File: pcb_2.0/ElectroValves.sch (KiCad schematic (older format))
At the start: 53 parts, among them P2 Conn_01x04_Female, Q1 PN2222, Q2 PN2222, Q6 PN2222, Q7 PN2222, U11 AQH3223AX, U12 AQH3223AX, U19 AQH3223AX, U20 AQH3223AX, U3 TLP240D, U4 TLP240D, U5 TLP240D, U6 TLP240D, U7 TLP240D, U8 TLP240D

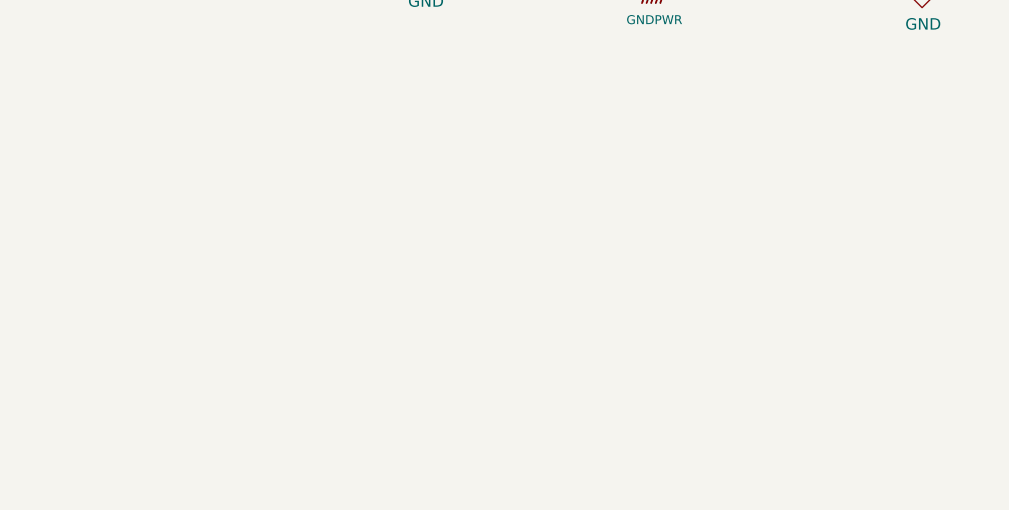
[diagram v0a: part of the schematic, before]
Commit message: driver for motor eliminated
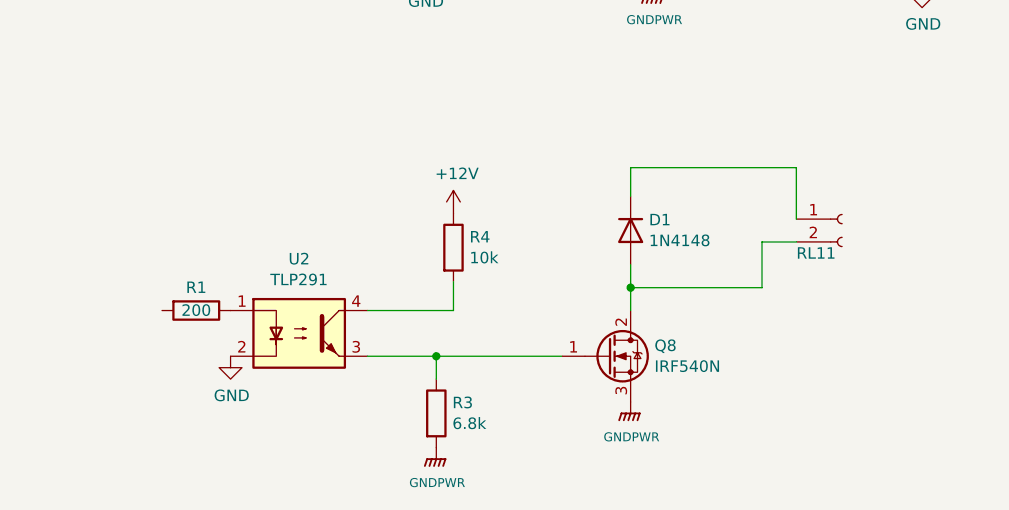
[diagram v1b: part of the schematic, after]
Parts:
- added D1: 1N4148, Diode_THT:D_DO-35_SOD27_P7.62mm_Horizontal, symbol Diode:1N4148
- added Q8: IRF540N, Package_TO_SOT_THT:TO-220-3_Vertical, symbol Transistor_FET:IRF540N
- added R1: 200, symbol Device:R
- added R3: 6.8k, symbol Device:R
- added R4: 10k, symbol Device:R
- added RL11: Conn_01x04_Female, Connector_Phoenix_MC:PhoenixContact_MC_1,5_2-G-3.81_1x02_P3.81mm_Horizontal, symbol BarrelConnector:Conn_01x02_Female
- added U2: TLP291, Package_SO:SOIC-4_4.55x2.6mm_P1.27mm, symbol Isolator:TLP291
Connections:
- net GND: now also U2.2
- net GNDPWR: now also Q8.3 (S), R3.2
- new net: R1.1, U2.1
- new net: Q8.1 (G), R3.1, U2.3
- new net: R4.2, U2.4
- new net: D1.2 (A), Q8.2 (D), RL11.2 (Pin_2)
- new net: D1.1 (K), RL11.1 (Pin_1)
- new net +12V: R4.1
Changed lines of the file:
@@
 $EndDescr
-$Comp
-L SolidStateRelay:TLP240D U3
-U 1 1 5E992915
-P 2850 1700
-F 0 "U3" H 2850 2025 50  0000 C CNN
-F 1 "TLP240D" H 2850 1934 50  0000 C CNN
-F 2 "SMD:TLP240D_TP1" H 2650 1500 50  0001 L CIN
-F 3 "https://toshiba.semicon-storage.com/info/docget.jsp?did=13993&prodName=TLP240D" H 2800 1700 50  0001 L CNN
-F 4 "TLP240D(TP1FCT-ND" H 2850 1700 50  0001 C CNN "DigiKey"
-	1    2850 1700
-	1    0    0    -1
-$EndComp
-$Comp
-L SolidStateRelay:TLP240D U4
-U 1 1 5E996503
-P 5025 1700
-F 0 "U4" H 5025 2025 50  0000 C CNN
-F 1 "TLP240D" H 5025 1934 50  0000 C CNN
-F 2 "SMD:TLP240D_TP1" H 4825 1500 50  0001 L CIN
-F 3 "" H 4975 1700 50  0001 L CNN
-F 4 "TLP240D(TP1FCT-ND" H 5025 1700 50  0001 C CNN "DigiKey"
-	1    5025 1700
-	1    0    0    -1
-$EndComp
-$Comp
-L SolidStateRelay:TLP240D U5
-U 1 1 5E9983C1
-P 2850 3475
-F 0 "U5" H 2850 3800 50  0000 C CNN
-F 1 "TLP240D" H 2850 3709 50  0000 C CNN
-F 2 "SMD:TLP240D_TP1" H 2650 3275 50  0001 L CIN
-F 3 "" H 2800 3475 50  0001 L CNN
-F 4 "TLP240D(TP1FCT-ND" H 2850 3475 50  0001 C CNN "DigiKey"
-	1    2850 3475
-	1    0    0    -1
-$EndComp
-$Comp
-L SolidStateRelay:TLP240D U6
-U 1 1 5E9983C7
-P 5025 3525
-F 0 "U6" H 5025 3850 50  0000 C CNN
-F 1 "TLP240D" H 5025 3759 50  0000 C CNN
-F 2 "SMD:TLP240D_TP1" H 4825 3325 50  0001 L CIN
-F 3 "" H 4975 3525 50  0001 L CNN
-F 4 "TLP240D(TP1FCT-ND" H 5025 3525 50  0001 C CNN "DigiKey"
-	1    5025 3525
-	1    0    0    -1
-$EndComp
 $Comp
 L SolidStateRelay:TLP240D U7
@@
 F 4 "TLP240D(TP1FCT-ND" H 2850 5200 50  0001 C CNN "DigiKey"
 	1    2850 5200
-	1    0    0    -1
-$EndComp
-$Comp
-L SolidStateRelay:TLP240D U8
-U 1 1 5E99CC75
-P 5025 5300
-F 0 "U8" H 5025 5625 50  0000 C CNN
-F 1 "TLP240D" H 5025 5534 50  0000 C CNN
-F 2 "SMD:TLP240D_TP1" H 4825 5100 50  0001 L CIN
-F 3 "" H 4975 5300 50  0001 L CNN
-F 4 "TLP240D(TP1FCT-ND" H 5025 5300 50  0001 C CNN "DigiKey"
-	1    5025 5300
 	1    0    0    -1
 $EndComp
@@
 Text Label 6925 5650 0    50   ~ 0
 R16
+$Comp
+L SolidStateRelay:TLP240D U8
+U 1 1 5E99CC75
+P 5025 5300
+F 0 "U8" H 5025 5625 50  0000 C CNN
+F 1 "TLP240D" H 5025 5534 50  0000 C CNN
+F 2 "SMD:TLP240D_TP1" H 4825 5100 50  0001 L CIN
+F 3 "" H 4975 5300 50  0001 L CNN
+F 4 "TLP240D(TP1FCT-ND" H 5025 5300 50  0001 C CNN "DigiKey"
+	1    5025 5300
+	1    0    0    -1
+$EndComp
+$Comp
+L SolidStateRelay:TLP240D U6
+U 1 1 5E9983C7
+P 5025 3525
+F 0 "U6" H 5025 3850 50  0000 C CNN
+F 1 "TLP240D" H 5025 3759 50  0000 C CNN
+F 2 "SMD:TLP240D_TP1" H 4825 3325 50  0001 L CIN
+F 3 "" H 4975 3525 50  0001 L CNN
+F 4 "TLP240D(TP1FCT-ND" H 5025 3525 50  0001 C CNN "DigiKey"
+	1    5025 3525
+	1    0    0    -1
+$EndComp
+$Comp
+L SolidStateRelay:TLP240D U4
+U 1 1 5E996503
+P 5025 1700
+F 0 "U4" H 5025 2025 50  0000 C CNN
+F 1 "TLP240D" H 5025 1934 50  0000 C CNN
+F 2 "SMD:TLP240D_TP1" H 4825 1500 50  0001 L CIN
+F 3 "" H 4975 1700 50  0001 L CNN
+F 4 "TLP240D(TP1FCT-ND" H 5025 1700 50  0001 C CNN "DigiKey"
+	1    5025 1700
+	1    0    0    -1
+$EndComp
+$Comp
+L SolidStateRelay:TLP240D U3
+U 1 1 5E992915
+P 2850 1700
+F 0 "U3" H 2850 2025 50  0000 C CNN
+F 1 "TLP240D" H 2850 1934 50  0000 C CNN
+F 2 "SMD:TLP240D_TP1" H 2650 1500 50  0001 L CIN
+F 3 "https://toshiba.semicon-storage.com/info/docget.jsp?did=13993&prodName=TLP240D" H 2800 1700 50  0001 L CNN
+F 4 "TLP240D(TP1FCT-ND" H 2850 1700 50  0001 C CNN "DigiKey"
+	1    2850 1700
+	1    0    0    -1
+$EndComp
+$Comp
+L SolidStateRelay:TLP240D U5
+U 1 1 5E9983C1
+P 2850 3475
+F 0 "U5" H 2850 3800 50  0000 C CNN
+F 1 "TLP240D" H 2850 3709 50  0000 C CNN
+F 2 "SMD:TLP240D_TP1" H 2650 3275 50  0001 L CIN
+F 3 "" H 2800 3475 50  0001 L CNN
+F 4 "TLP240D(TP1FCT-ND" H 2850 3475 50  0001 C CNN "DigiKey"
+	1    2850 3475
+	1    0    0    -1
+$EndComp
+$Comp
+L Isolator:TLP291 U2
+U 1 1 6162DFAF
+P 2000 6925
+F 0 "U2" H 2000 7250 50  0000 C CNN
+F 1 "TLP291" H 2000 7159 50  0000 C CNN
+F 2 "Package_SO:SOIC-4_4.55x2.6mm_P1.27mm" H 1800 6725 50  0001 L CIN
+F 3 "https://toshiba.semicon-storage.com/info/docget.jsp?did=12884&prodName=TLP291" H 2000 6925 50  0001 L CNN
+	1    2000 6925
+	1    0    0    -1
+$EndComp
+$Comp
+L Transistor_FET:IRF540N Q8
+U 1 1 616387FB
+P 3350 7025
+F 0 "Q8" H 3554 7071 50  0000 L CNN
+F 1 "IRF540N" H 3554 6980 50  0000 L CNN
+F 2 "Package_TO_SOT_THT:TO-220-3_Vertical" H 3600 6950 50  0001 L CIN
+F 3 "http://www.irf.com/product-info/datasheets/data/irf540n.pdf" H 3350 7025 50  0001 L CNN
+	1    3350 7025
+	1    0    0    -1
+$EndComp
+$Comp
+L Diode:1N4148 D1
+U 1 1 6163B9B9
+P 3450 6475
+F 0 "D1" V 3404 6555 50  0000 L CNN
+F 1 "1N4148" V 3495 6555 50  0000 L CNN
+F 2 "Diode_THT:D_DO-35_SOD27_P7.62mm_Horizontal" H 3450 6300 50  0001 C CNN
+F 3 "https://assets.nexperia.com/documents/data-sheet/1N4148_1N4448.pdf" H 3450 6475 50  0001 C CNN
+	1    3450 6475
+	0    1    1    0
+$EndComp
+$Comp
+L power:GNDPWR #PWR0113
+U 1 1 6164B980
+P 3450 7225
+F 0 "#PWR0113" H 3450 7025 50  0001 C CNN
+F 1 "GNDPWR" H 3454 7071 39  0000 C CNN
+F 2 "" H 3450 7175 50  0001 C CNN
+F 3 "" H 3450 7175 50  0001 C CNN
+	1    3450 7225
+	1    0    0    -1
+$EndComp
+$Comp
+L BarrelConnector:Conn_01x02_Female RL11
+U 1 1 616621F1
+P 4375 6425
+F 0 "RL11" H 4175 6275 50  0000 L CNN
+F 1 "Conn_01x04_Female" H 3925 6675 50  0001 L CNN
+F 2 "Connector_Phoenix_MC:PhoenixContact_MC_1,5_2-G-3.81_1x02_P3.81mm_Horizontal" H 4375 6425 50  0001 C CNN
+F 3 "~" H 4375 6425 50  0001 C CNN
+F 4 "277-1206-ND" H 4375 6425 50  0001 C CNN "DigiKey"
+F 5 "277-1161-ND" H 4375 6425 50  0001 C CNN "DigiKey2"
+	1    4375 6425
+	1    0    0    -1
+$EndComp
+Wire Wire Line
+	3450 6325 3450 6200
+Wire Wire Line
+	3450 6200 4175 6200
+Wire Wire Line
+	4175 6200 4175 6425
+Wire Wire Line
+	3450 6625 3450 6725
+Wire Wire Line
+	3450 6725 4025 6725
+Wire Wire Line
+	4025 6725 4025 6525
+Wire Wire Line
+	4025 6525 4175 6525
+Connection ~ 3450 6725
+Wire Wire Line
+	3450 6725 3450 6825
+Wire Wire Line
+	2300 7025 2600 7025
+$Comp
+L power:+12V #PWR0114
+U 1 1 616BA2C0
+P 2675 6400
+F 0 "#PWR0114" H 2675 6250 50  0001 C CNN
+F 1 "+12V" H 2690 6573 50  0000 C CNN
+F 2 "" H 2675 6400 50  0001 C CNN
+F 3 "" H 2675 6400 50  0001 C CNN
+	1    2675 6400
+	1    0    0    -1
+$EndComp
+$Comp
+L Device:R R4
+U 1 1 616C1442
+P 2675 6550
+F 0 "R4" H 2745 6596 50  0000 L CNN
+F 1 "10k" H 2745 6505 50  0000 L CNN
+F 2 "" V 2605 6550 50  0001 C CNN
+F 3 "~" H 2675 6550 50  0001 C CNN
+	1    2675 6550
+	1    0    0    -1
+$EndComp
+$Comp
+L Device:R R3
+U 1 1 616C1B24
+P 2600 7275
+F 0 "R3" H 2670 7321 50  0000 L CNN
+F 1 "6.8k" H 2670 7230 50  0000 L CNN
+F 2 "" V 2530 7275 50  0001 C CNN
+F 3 "~" H 2600 7275 50  0001 C CNN
+	1    2600 7275
+	1    0    0    -1
+$EndComp
+$Comp
+L power:GNDPWR #PWR0115
+U 1 1 616C3D92
+P 2600 7425
+F 0 "#PWR0115" H 2600 7225 50  0001 C CNN
+F 1 "GNDPWR" H 2604 7271 39  0000 C CNN
+F 2 "" H 2600 7375 50  0001 C CNN
+F 3 "" H 2600 7375 50  0001 C CNN
+	1    2600 7425
+	1    0    0    -1
+$EndComp
+Wire Wire Line
+	2300 6825 2675 6825
+Wire Wire Line
+	2675 6825 2675 6700
+Wire Wire Line
+	2600 7125 2600 7025
+Connection ~ 2600 7025
+Wire Wire Line
+	2600 7025 3150 7025
+$Comp
+L Device:R R1
+U 1 1 616DD315
+P 1550 6825
+F 0 "R1" V 1450 6825 50  0000 C CNN
+F 1 "200" V 1550 6825 50  0000 C CNN
+F 2 "" V 1480 6825 50  0001 C CNN
+F 3 "~" H 1550 6825 50  0001 C CNN
+	1    1550 6825
+	0    1    1    0
+$EndComp
+$Comp
+L power:GND #PWR0141
+U 1 1 616DE2DB
+P 1700 7025
+F 0 "#PWR0141" H 1700 6775 50  0001 C CNN
+F 1 "GND" H 1705 6852 50  0000 C CNN
+F 2 "" H 1700 7025 50  0001 C CNN
+F 3 "" H 1700 7025 50  0001 C CNN
+	1    1700 7025
+	1    0    0    -1
+$EndComp
 Wire Bus Line
 	1000 700  1000 1650

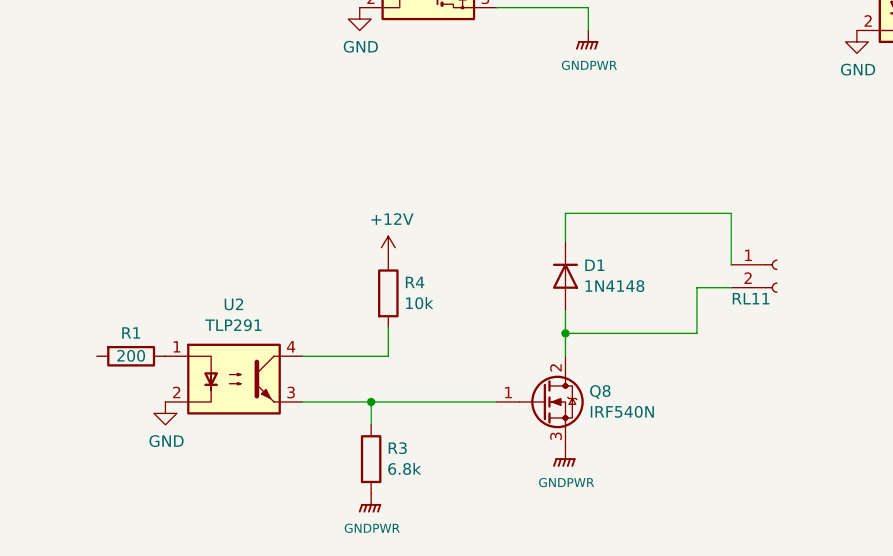
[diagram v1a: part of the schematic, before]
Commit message: Modified sensor modules and created module for 403-SFM3020 sensor
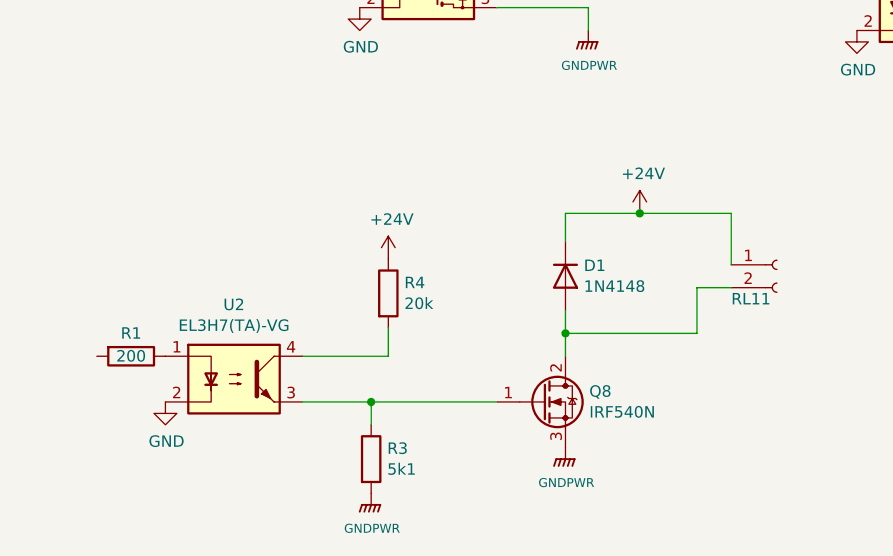
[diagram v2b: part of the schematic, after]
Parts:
- R1: DigiKey (none) -> P200LCT-ND
- R3: value 6.8k -> 5k1
- R4: value 10k -> 20k
- U2: value TLP291 -> EL3H7(TA)-VG; DigiKey (none) -> 160-1337-1-ND
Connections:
- net +12V is gone; now on net +24V: R4.1
- net +24V: now reaches D1.1 (K), RL11.1 (Pin_1)
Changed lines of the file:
@@
 P 2000 6925
 F 0 "U2" H 2000 7250 50  0000 C CNN
-F 1 "TLP291" H 2000 7159 50  0000 C CNN
+F 1 "EL3H7(TA)-VG" H 2000 7159 50  0000 C CNN
 F 2 "Package_SO:SOIC-4_4.55x2.6mm_P1.27mm" H 1800 6725 50  0001 L CIN
 F 3 "https://toshiba.semicon-storage.com/info/docget.jsp?did=12884&prodName=TLP291" H 2000 6925 50  0001 L CNN
+F 4 "160-1337-1-ND" H 2000 6925 50  0001 C CNN "DigiKey"
 	1    2000 6925
 	1    0    0    -1
@@
 	3450 6325 3450 6200
 Wire Wire Line
-	3450 6200 4175 6200
+	3450 6200 3775 6200
 Wire Wire Line
 	4175 6200 4175 6425
@@
 	2300 7025 2600 7025
 $Comp
-L power:+12V #PWR0114
-U 1 1 616BA2C0
-P 2675 6400
-F 0 "#PWR0114" H 2675 6250 50  0001 C CNN
-F 1 "+12V" H 2690 6573 50  0000 C CNN
-F 2 "" H 2675 6400 50  0001 C CNN
-F 3 "" H 2675 6400 50  0001 C CNN
-	1    2675 6400
-	1    0    0    -1
-$EndComp
-$Comp
 L Device:R R4
 U 1 1 616C1442
 P 2675 6550
 F 0 "R4" H 2745 6596 50  0000 L CNN
-F 1 "10k" H 2745 6505 50  0000 L CNN
+F 1 "20k" H 2745 6505 50  0000 L CNN
 F 2 "" V 2605 6550 50  0001 C CNN
 F 3 "~" H 2675 6550 50  0001 C CNN
@@
 P 2600 7275
 F 0 "R3" H 2670 7321 50  0000 L CNN
-F 1 "6.8k" H 2670 7230 50  0000 L CNN
+F 1 "5k1" H 2670 7230 50  0000 L CNN
 F 2 "" V 2530 7275 50  0001 C CNN
 F 3 "~" H 2600 7275 50  0001 C CNN
@@
 F 2 "" V 1480 6825 50  0001 C CNN
 F 3 "~" H 1550 6825 50  0001 C CNN
+F 4 "P200LCT-ND" V 1550 6825 50  0001 C CNN "DigiKey"
 	1    1550 6825
 	0    1    1    0
@@
 	1    0    0    -1
 $EndComp
+$Comp
+L power:+24V #PWR?
+U 1 1 61A1E826
+P 2675 6400
+F 0 "#PWR?" H 2675 6250 50  0001 C CNN
+F 1 "+24V" H 2690 6573 50  0000 C CNN
+F 2 "" H 2675 6400 50  0001 C CNN
+F 3 "" H 2675 6400 50  0001 C CNN
+	1    2675 6400
+	1    0    0    -1
+$EndComp
+$Comp
+L power:+24V #PWR?
+U 1 1 61A410D5
+P 3775 6200
+F 0 "#PWR?" H 3775 6050 50  0001 C CNN
+F 1 "+24V" H 3790 6373 50  0000 C CNN
+F 2 "" H 3775 6200 50  0001 C CNN
+F 3 "" H 3775 6200 50  0001 C CNN
+	1    3775 6200
+	1    0    0    -1
+$EndComp
+Connection ~ 3775 6200
+Wire Wire Line
+	3775 6200 4175 6200
 Wire Bus Line
 	1000 700  1000 1650
